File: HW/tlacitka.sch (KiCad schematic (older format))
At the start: 22 parts, among them SW10 button, SW11 button, SW12 button, SW2 button, SW3 button, SW4 button, SW5 button, SW6 button, SW7 button, SW8 button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

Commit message: V1.1 change SMD buttons, add diode on VCC
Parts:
- SW10, SW11, SW12, SW2, SW3, SW4, SW5, SW6, SW7, SW8, SW9: footprint Button_Switch_THT:SW_PUSH_6mm -> my_library:Tactile_switch; LCSC ručně -> C318887

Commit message: repair footprint of DIP and USB micro, change buttons with higher fretboard
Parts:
- SW10, SW11, SW12, SW2, SW3, SW4, SW5, SW6, SW7, SW8, SW9: LCSC C318887 -> C318886
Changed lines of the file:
@@
 F 2 "my_library:Tactile_switch" H 4850 6200 50  0001 C CNN
 F 3 "~" H 4850 6200 50  0001 C CNN
-F 4 "C318887" H 4850 6000 50  0001 C CNN "LCSC"
+F 4 "C318886" H 4850 6000 50  0001 C CNN "LCSC"
 F 5 "0;0;0" H 4850 6000 50  0001 C CNN "JLCPCB_CORRECTION"
 	1    4850 6000
@@
 F 2 "my_library:Tactile_switch" H 7000 1800 50  0001 C CNN
 F 3 "~" H 7000 1800 50  0001 C CNN
-F 4 "C318887" H 7000 1600 50  0001 C CNN "LCSC"
+F 4 "C318886" H 7000 1600 50  0001 C CNN "LCSC"
 F 5 "0;0;0" H 7000 1600 50  0001 C CNN "JLCPCB_CORRECTION"
 	1    7000 1600
@@
 F 2 "my_library:Tactile_switch" H 7000 3450 50  0001 C CNN
 F 3 "~" H 7000 3450 50  0001 C CNN
-F 4 "C318887" H 7000 3250 50  0001 C CNN "LCSC"
+F 4 "C318886" H 7000 3250 50  0001 C CNN "LCSC"
 F 5 "0;0;0" H 7000 3250 50  0001 C CNN "JLCPCB_CORRECTION"
 	1    7000 3250
@@
 F 2 "my_library:Tactile_switch" H 7000 2600 50  0001 C CNN
 F 3 "~" H 7000 2600 50  0001 C CNN
-F 4 "C318887" H 7000 2400 50  0001 C CNN "LCSC"
+F 4 "C318886" H 7000 2400 50  0001 C CNN "LCSC"
 F 5 "0;0;0" H 7000 2400 50  0001 C CNN "JLCPCB_CORRECTION"
 	1    7000 2400
@@
 F 2 "my_library:Tactile_switch" H 4850 3450 50  0001 C CNN
 F 3 "~" H 4850 3450 50  0001 C CNN
-F 4 "C318887" H 4850 3250 50  0001 C CNN "LCSC"
+F 4 "C318886" H 4850 3250 50  0001 C CNN "LCSC"
 F 5 "0;0;0" H 4850 3250 50  0001 C CNN "JLCPCB_CORRECTION"
 	1    4850 3250
@@
 F 2 "my_library:Tactile_switch" H 4800 2600 50  0001 C CNN
 F 3 "~" H 4800 2600 50  0001 C CNN
-F 4 "C318887" H 4800 2400 50  0001 C CNN "LCSC"
+F 4 "C318886" H 4800 2400 50  0001 C CNN "LCSC"
 F 5 "0;0;0" H 4800 2400 50  0001 C CNN "JLCPCB_CORRECTION"
 	1    4800 2400
@@
 F 2 "my_library:Tactile_switch" H 7000 5400 50  0001 C CNN
 F 3 "~" H 7000 5400 50  0001 C CNN
-F 4 "C318887" H 7000 5200 50  0001 C CNN "LCSC"
+F 4 "C318886" H 7000 5200 50  0001 C CNN "LCSC"
 F 5 "0;0;0" H 7000 5200 50  0001 C CNN "JLCPCB_CORRECTION"
 	1    7000 5200
@@
 F 2 "my_library:Tactile_switch" H 7000 4550 50  0001 C CNN
 F 3 "~" H 7000 4550 50  0001 C CNN
-F 4 "C318887" H 7000 4350 50  0001 C CNN "LCSC"
+F 4 "C318886" H 7000 4350 50  0001 C CNN "LCSC"
 F 5 "0;0;0" H 7000 4350 50  0001 C CNN "JLCPCB_CORRECTION"
 	1    7000 4350
@@
 F 2 "my_library:Tactile_switch" H 4850 5400 50  0001 C CNN
 F 3 "~" H 4850 5400 50  0001 C CNN
-F 4 "C318887" H 4850 5200 50  0001 C CNN "LCSC"
+F 4 "C318886" H 4850 5200 50  0001 C CNN "LCSC"
 F 5 "0;0;0" H 4850 5200 50  0001 C CNN "JLCPCB_CORRECTION"
 	1    4850 5200
@@
 F 2 "my_library:Tactile_switch" H 4800 4550 50  0001 C CNN
 F 3 "~" H 4800 4550 50  0001 C CNN
-F 4 "C318887" H 4800 4350 50  0001 C CNN "LCSC"
+F 4 "C318886" H 4800 4350 50  0001 C CNN "LCSC"
 F 5 "0;0;0" H 4800 4350 50  0001 C CNN "JLCPCB_CORRECTION"
 	1    4800 4350
@@
 F 2 "my_library:Tactile_switch" H 4800 1800 50  0001 C CNN
 F 3 "~" H 4800 1800 50  0001 C CNN
-F 4 "C318887" H 4800 1600 50  0001 C CNN "LCSC"
+F 4 "C318886" H 4800 1600 50  0001 C CNN "LCSC"
 F 5 "0;0;0" H 4800 1600 50  0001 C CNN "JLCPCB_CORRECTION"
 	1    4800 1600

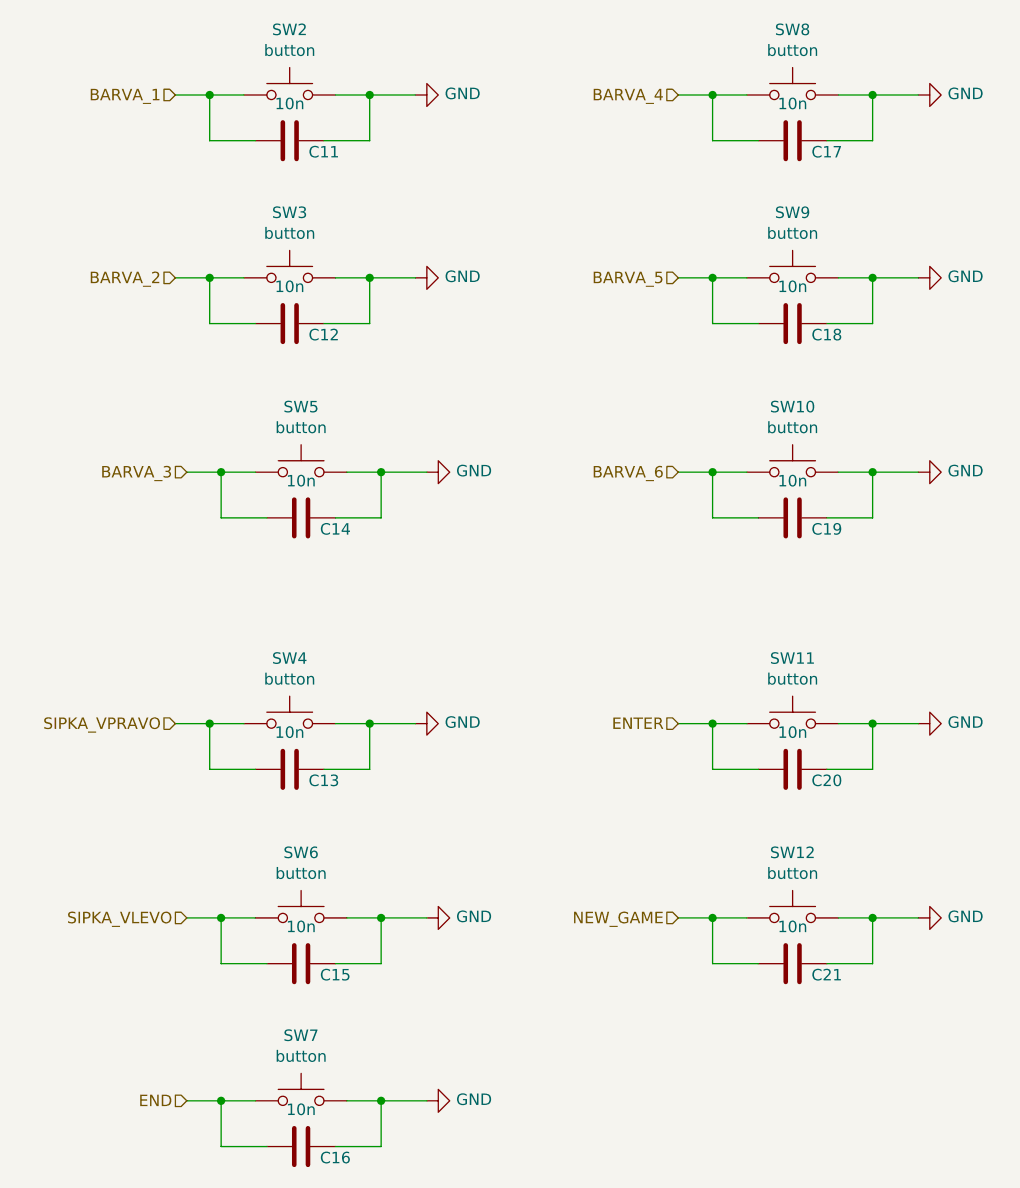
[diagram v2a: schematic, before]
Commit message: make schematic beautiful (for printing)
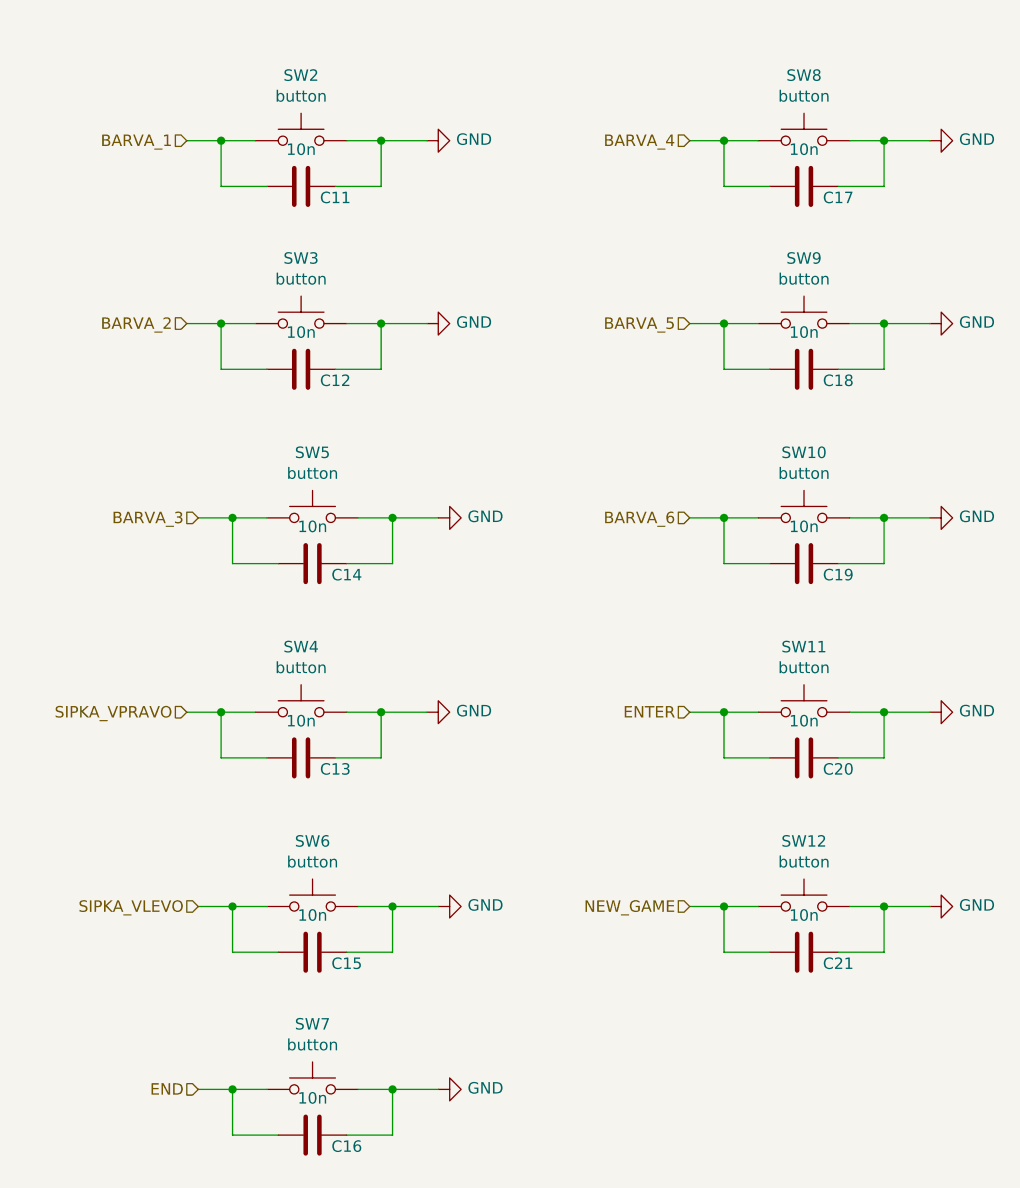
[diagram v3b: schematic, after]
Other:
- moved on the sheet: C11, C12, C13, C14, C15, C16, C17, C18, C19, C20, C21, SW10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
